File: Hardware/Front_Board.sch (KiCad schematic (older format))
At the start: 15 parts, among them J4 Camera, J5 Motherboard_Right, Q1 DMG3414U

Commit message: [Hardware] Renamed 'camera board' to 'front board' as this board is not only carrying the camera.
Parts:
- J4: value Camera -> Front
- J5: value Motherboard_Right -> Front
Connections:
- net CAMERA_BOARD_LDR renamed FRONT_BOARD_LDR
- net CAMERA_BOARD_LEDS renamed FRONT_BOARD_LEDS
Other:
- note added: "Separate front board."
- note removed: "Camera separate board."
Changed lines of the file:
@@
 P 7350 3850
 F 0 "J5" H 7429 3705 50  0000 L CNN
-F 1 "Motherboard_Right" H 7429 3796 50  0000 L CNN
+F 1 "Front" H 7429 3796 50  0000 L CNN
 F 2 "Connector_PinSocket_2.54mm:PinSocket_1x04_P2.54mm_Vertical" H 7350 3850 50  0001 C CNN
 F 3 "~" H 7350 3850 50  0001 C CNN
@@
 	8200 3300 8450 3300
 Text GLabel 7800 3750 2    50   UnSpc ~ 0
-CAMERA_BOARD_LDR
+FRONT_BOARD_LDR
 Wire Wire Line
 	7800 3750 7550 3750
@@
 Wire Notes Line
 	2500 2550 2500 5250
-Text Notes 5150 5150 0    50   ~ 0
-Camera separate board.
+Text Notes 5350 5150 0    50   ~ 0
+Separate front board.
 Wire Wire Line
 	2850 4700 2850 3900
@@
 	8850 4100 8850 4150
 Text GLabel 9100 4100 2    50   Input ~ 0
-CAMERA_BOARD_LEDS
+FRONT_BOARD_LEDS
 Wire Wire Line
 	8850 4100 9100 4100
@@
 P 5350 3750
 F 0 "J4" H 5430 3787 50  0000 L CNN
-F 1 "Camera" H 5430 3696 50  0000 L CNN
+F 1 "Front" H 5430 3696 50  0000 L CNN
 F 2 "Connector_PinHeader_2.54mm:PinHeader_1x04_P2.54mm_Vertical" H 5350 3750 50  0001 C CNN
 F 3 "~" H 5350 3750 50  0001 C CNN

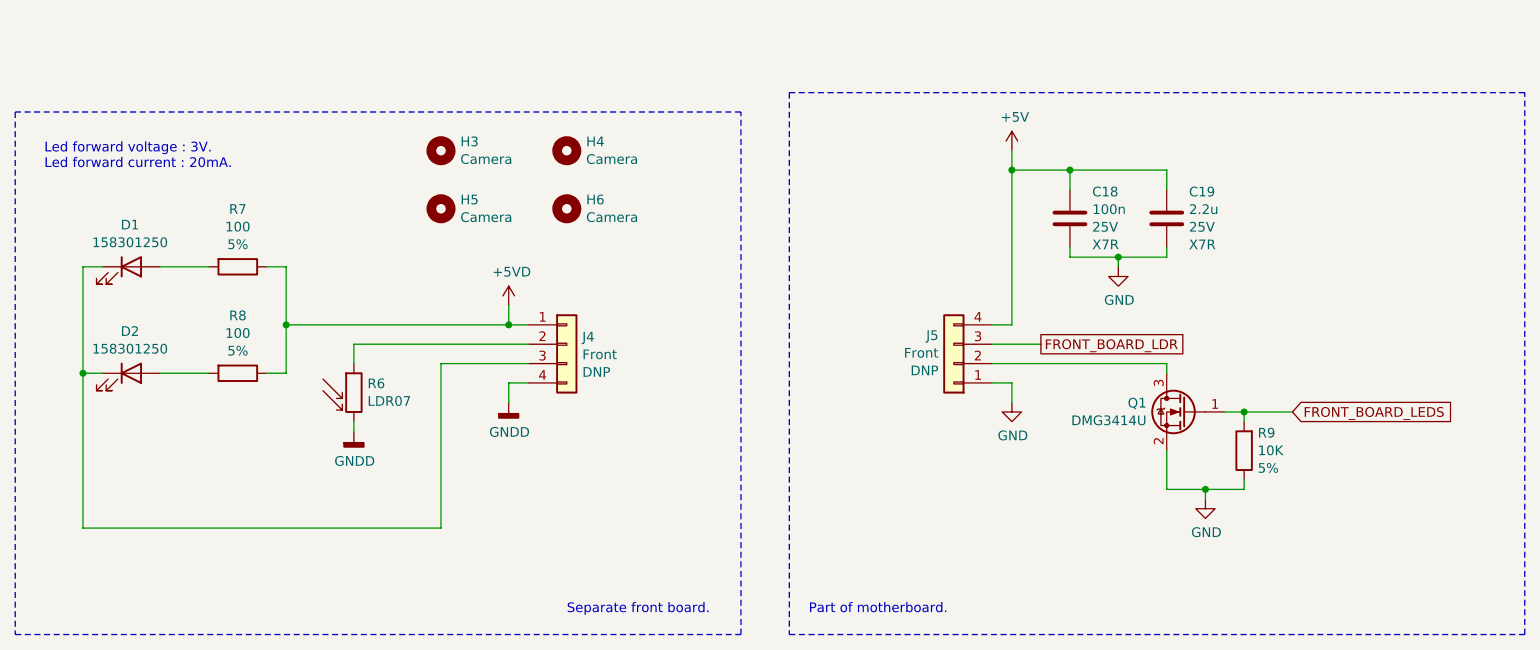
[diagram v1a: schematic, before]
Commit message: [Hardware] Added two more leds for a better night lighting.
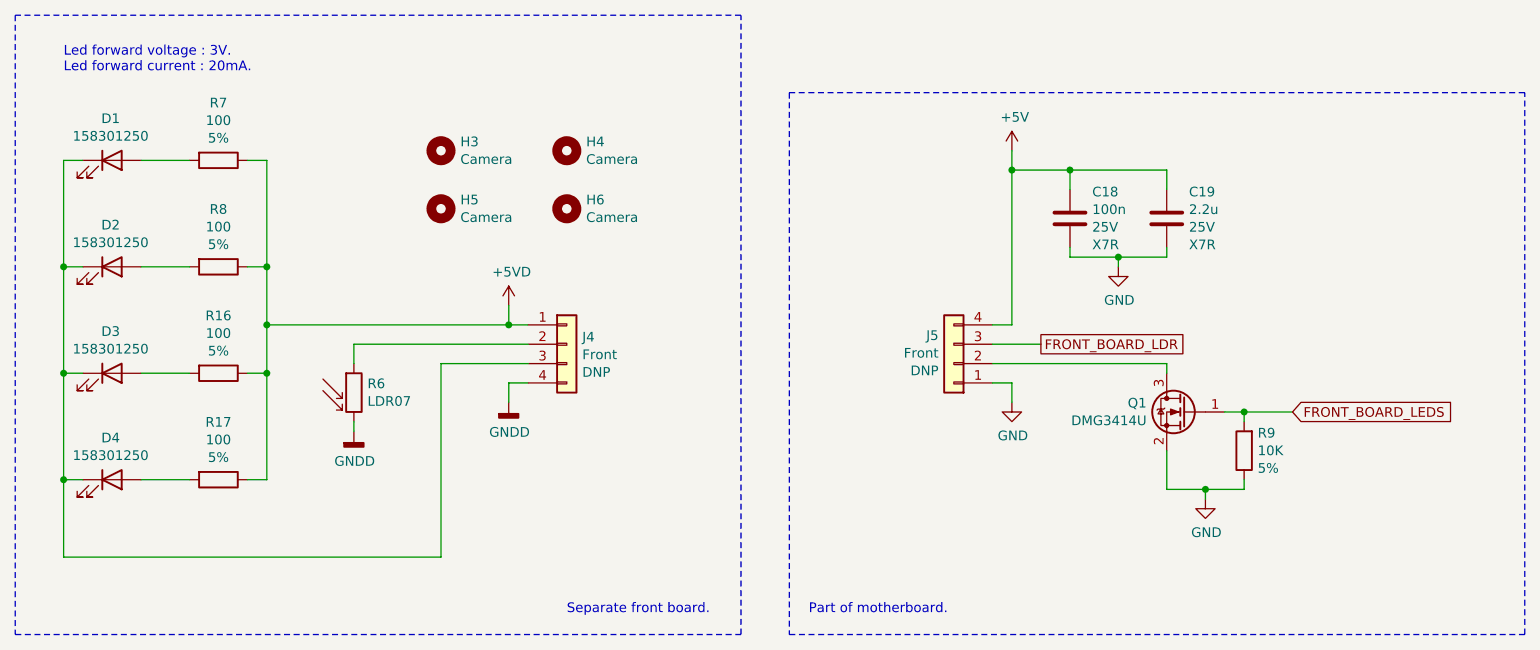
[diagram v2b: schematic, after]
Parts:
- added D3, D4: 158301250, 158301250:158301250, symbol Device:LED
- added R16, R17: 100, Resistor_SMD:R_1206_3216Metric_Pad1.42x1.75mm_HandSolder, symbol Device:R
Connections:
- net +5VD: now also R16.1, R17.1
- net at D1.1 (K), D2.1 (K), J4.3 (Pin_3): now also D3.1 (K), D4.1 (K)
- new net: D3.2 (A), R16.2
- new net: D4.2 (A), R17.2
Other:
- moved on the sheet: D1, D2, R7, R8
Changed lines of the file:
@@
 L Device:LED D1
 U 1 1 5F289A86
-P 3100 3350
-F 0 "D1" H 3093 3566 50  0000 C CNN
-F 1 "158301250" H 3093 3475 50  0000 C CNN
-F 2 "158301250:158301250" H 3100 3350 50  0001 C CNN
-F 3 "~" H 3100 3350 50  0001 C CNN
-	1    3100 3350
+P 3000 2800
+F 0 "D1" H 2993 3016 50  0000 C CNN
+F 1 "158301250" H 2993 2925 50  0000 C CNN
+F 2 "158301250:158301250" H 3000 2800 50  0001 C CNN
+F 3 "~" H 3000 2800 50  0001 C CNN
+	1    3000 2800
 	1    0    0    -1
 $EndComp
@@
 L Device:LED D2
 U 1 1 5F28F949
-P 3100 3900
-F 0 "D2" H 3093 4116 50  0000 C CNN
-F 1 "158301250" H 3093 4025 50  0000 C CNN
-F 2 "158301250:158301250" H 3100 3900 50  0001 C CNN
-F 3 "~" H 3100 3900 50  0001 C CNN
-	1    3100 3900
+P 3000 3350
+F 0 "D2" H 2993 3566 50  0000 C CNN
+F 1 "158301250" H 2993 3475 50  0000 C CNN
+F 2 "158301250:158301250" H 3000 3350 50  0001 C CNN
+F 3 "~" H 3000 3350 50  0001 C CNN
+	1    3000 3350
 	1    0    0    -1
 $EndComp
@@
 Wire Wire Line
 	5050 3650 5150 3650
-Connection ~ 5050 3650
-Wire Wire Line
-	2950 3900 2850 3900
-Wire Wire Line
-	2850 3900 2850 3350
-Wire Wire Line
-	2850 3350 2950 3350
-Text Notes 2650 2850 0    50   ~ 0
+Wire Wire Line
+	2850 3350 2750 3350
+Wire Wire Line
+	2750 3350 2750 2800
+Wire Wire Line
+	2750 2800 2850 2800
+Text Notes 2750 2350 0    50   ~ 0
 Led forward voltage : 3V.\nLed forward current : 20mA.
 $Comp
 L Device:R R7
 U 1 1 5F2D70A9
-P 3650 3350
-F 0 "R7" V 3353 3350 50  0000 C CNN
-F 1 "100" V 3444 3350 50  0000 C CNN
-F 2 "Resistor_SMD:R_1206_3216Metric_Pad1.42x1.75mm_HandSolder" V 3580 3350 50  0001 C CNN
-F 3 "~" H 3650 3350 50  0001 C CNN
-F 4 "5%" V 3535 3350 50  0000 C CNN "Value2"
-	1    3650 3350
+P 3550 2800
+F 0 "R7" V 3253 2800 50  0000 C CNN
+F 1 "100" V 3344 2800 50  0000 C CNN
+F 2 "Resistor_SMD:R_1206_3216Metric_Pad1.42x1.75mm_HandSolder" V 3480 2800 50  0001 C CNN
+F 3 "~" H 3550 2800 50  0001 C CNN
+F 4 "5%" V 3435 2800 50  0000 C CNN "Value2"
+	1    3550 2800
 	0    1    1    0
 $EndComp
@@
 L Device:R R8
 U 1 1 5F2DA263
-P 3650 3900
-F 0 "R8" V 3353 3900 50  0000 C CNN
-F 1 "100" V 3444 3900 50  0000 C CNN
-F 2 "Resistor_SMD:R_1206_3216Metric_Pad1.42x1.75mm_HandSolder" V 3580 3900 50  0001 C CNN
-F 3 "~" H 3650 3900 50  0001 C CNN
-F 4 "5%" V 3535 3900 50  0000 C CNN "Value2"
-	1    3650 3900
+P 3550 3350
+F 0 "R8" V 3253 3350 50  0000 C CNN
+F 1 "100" V 3344 3350 50  0000 C CNN
+F 2 "Resistor_SMD:R_1206_3216Metric_Pad1.42x1.75mm_HandSolder" V 3480 3350 50  0001 C CNN
+F 3 "~" H 3550 3350 50  0001 C CNN
+F 4 "5%" V 3435 3350 50  0000 C CNN "Value2"
+	1    3550 3350
 	0    1    1    0
 $EndComp
 Wire Wire Line
-	3250 3350 3500 3350
-Wire Wire Line
-	3250 3900 3500 3900
-Wire Wire Line
-	3800 3350 3900 3350
-Wire Wire Line
-	3900 3350 3900 3650
-Wire Wire Line
-	3900 3900 3800 3900
-Wire Wire Line
-	3900 3650 5050 3650
-Connection ~ 3900 3650
-Wire Wire Line
-	3900 3650 3900 3900
+	3150 2800 3400 2800
+Wire Wire Line
+	3150 3350 3400 3350
+Wire Wire Line
+	3700 2800 3800 2800
+Wire Wire Line
+	3800 3350 3700 3350
 $Comp
 L Mechanical:MountingHole H3
@@
 	2500 5250 6250 5250
 Wire Notes Line
-	6250 5250 6250 2550
-Wire Notes Line
-	6250 2550 2500 2550
-Wire Notes Line
-	2500 2550 2500 5250
+	6250 5250 6250 2050
+Wire Notes Line
+	6250 2050 2500 2050
+Wire Notes Line
+	2500 2050 2500 5250
 Text Notes 5350 5150 0    50   ~ 0
 Separate front board.
-Wire Wire Line
-	2850 4700 2850 3900
-Connection ~ 2850 3900
+Connection ~ 2750 3350
 $Comp
 L Transistor_FET:DMG3414U Q1
@@
 	4250 3750 4250 3850
 Wire Wire Line
-	4700 3850 4700 4700
-Wire Wire Line
 	4700 3850 5150 3850
-Wire Wire Line
-	4700 4700 2850 4700
 Wire Wire Line
 	7650 2750 7650 2850
@@
 Wire Wire Line
 	7650 3950 7650 4050
+$Comp
+L Device:LED D3
+U 1 1 5F22A727
+P 3000 3900
+F 0 "D3" H 2993 4116 50  0000 C CNN
+F 1 "158301250" H 2993 4025 50  0000 C CNN
+F 2 "158301250:158301250" H 3000 3900 50  0001 C CNN
+F 3 "~" H 3000 3900 50  0001 C CNN
+	1    3000 3900
+	1    0    0    -1
+$EndComp
+$Comp
+L Device:LED D4
+U 1 1 5F22A72D
+P 3000 4450
+F 0 "D4" H 2993 4666 50  0000 C CNN
+F 1 "158301250" H 2993 4575 50  0000 C CNN
+F 2 "158301250:158301250" H 3000 4450 50  0001 C CNN
+F 3 "~" H 3000 4450 50  0001 C CNN
+	1    3000 4450
+	1    0    0    -1
+$EndComp
+Wire Wire Line
+	2850 4450 2750 4450
+$Comp
+L Device:R R16
+U 1 1 5F22A736
+P 3550 3900
+F 0 "R16" V 3253 3900 50  0000 C CNN
+F 1 "100" V 3344 3900 50  0000 C CNN
+F 2 "Resistor_SMD:R_1206_3216Metric_Pad1.42x1.75mm_HandSolder" V 3480 3900 50  0001 C CNN
+F 3 "~" H 3550 3900 50  0001 C CNN
+F 4 "5%" V 3435 3900 50  0000 C CNN "Value2"
+	1    3550 3900
+	0    1    1    0
+$EndComp
+$Comp
+L Device:R R17
+U 1 1 5F22A73D
+P 3550 4450
+F 0 "R17" V 3253 4450 50  0000 C CNN
+F 1 "100" V 3344 4450 50  0000 C CNN
+F 2 "Resistor_SMD:R_1206_3216Metric_Pad1.42x1.75mm_HandSolder" V 3480 4450 50  0001 C CNN
+F 3 "~" H 3550 4450 50  0001 C CNN
+F 4 "5%" V 3435 4450 50  0000 C CNN "Value2"
+	1    3550 4450
+	0    1    1    0
+$EndComp
+Wire Wire Line
+	3150 3900 3400 3900
+Wire Wire Line
+	3150 4450 3400 4450
+Wire Wire Line
+	3700 3900 3800 3900
+Wire Wire Line
+	3800 4450 3700 4450
+Wire Wire Line
+	2850 3900 2750 3900
+Connection ~ 2750 3900
+Wire Wire Line
+	2750 3900 2750 3350
+Wire Wire Line
+	3800 3350 3800 3650
+Connection ~ 3800 3350
+Wire Wire Line
+	3800 3900 3800 4450
+Connection ~ 3800 3900
+Wire Wire Line
+	2750 3900 2750 4450
+Wire Wire Line
+	3800 2800 3800 3350
+Connection ~ 5050 3650
+Wire Wire Line
+	3800 3650 5050 3650
+Connection ~ 3800 3650
+Wire Wire Line
+	3800 3650 3800 3900
+Wire Wire Line
+	2750 4450 2750 4850
+Wire Wire Line
+	2750 4850 4700 4850
+Wire Wire Line
+	4700 3850 4700 4850
+Connection ~ 2750 4450
 $EndSCHEMATC

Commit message: [Hardware] Added front board mounting holes.
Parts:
- added H11, H12: Front_Board, MountingHole:MountingHole_4.3mm_M4, symbol Mechanical:MountingHole
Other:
- moved on the sheet: H3, H4, H5, H6
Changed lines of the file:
@@
 L Mechanical:MountingHole H3
 U 1 1 5F2EC62F
-P 4700 2750
-F 0 "H3" H 4800 2796 50  0000 L CNN
-F 1 "Camera" H 4800 2705 50  0000 L CNN
-F 2 "MountingHole:MountingHole_2.2mm_M2" H 4700 2750 50  0001 C CNN
-F 3 "~" H 4700 2750 50  0001 C CNN
-	1    4700 2750
+P 4500 2350
+F 0 "H3" H 4600 2396 50  0000 L CNN
+F 1 "Camera" H 4600 2305 50  0000 L CNN
+F 2 "MountingHole:MountingHole_2.2mm_M2" H 4500 2350 50  0001 C CNN
+F 3 "~" H 4500 2350 50  0001 C CNN
+	1    4500 2350
 	1    0    0    -1
 $EndComp
@@
 L Mechanical:MountingHole H4
 U 1 1 5F2F030A
-P 5350 2750
-F 0 "H4" H 5450 2796 50  0000 L CNN
-F 1 "Camera" H 5450 2705 50  0000 L CNN
-F 2 "MountingHole:MountingHole_2.2mm_M2" H 5350 2750 50  0001 C CNN
-F 3 "~" H 5350 2750 50  0001 C CNN
-	1    5350 2750
+P 5250 2350
+F 0 "H4" H 5350 2396 50  0000 L CNN
+F 1 "Camera" H 5350 2305 50  0000 L CNN
+F 2 "MountingHole:MountingHole_2.2mm_M2" H 5250 2350 50  0001 C CNN
+F 3 "~" H 5250 2350 50  0001 C CNN
+	1    5250 2350
 	1    0    0    -1
 $EndComp
@@
 L Mechanical:MountingHole H5
 U 1 1 5F2F0621
-P 4700 3050
-F 0 "H5" H 4800 3096 50  0000 L CNN
-F 1 "Camera" H 4800 3005 50  0000 L CNN
-F 2 "MountingHole:MountingHole_2.2mm_M2" H 4700 3050 50  0001 C CNN
-F 3 "~" H 4700 3050 50  0001 C CNN
-	1    4700 3050
+P 4500 2650
+F 0 "H5" H 4600 2696 50  0000 L CNN
+F 1 "Camera" H 4600 2605 50  0000 L CNN
+F 2 "MountingHole:MountingHole_2.2mm_M2" H 4500 2650 50  0001 C CNN
+F 3 "~" H 4500 2650 50  0001 C CNN
+	1    4500 2650
 	1    0    0    -1
 $EndComp
@@
 L Mechanical:MountingHole H6
 U 1 1 5F2F098F
-P 5350 3050
-F 0 "H6" H 5450 3096 50  0000 L CNN
-F 1 "Camera" H 5450 3005 50  0000 L CNN
-F 2 "MountingHole:MountingHole_2.2mm_M2" H 5350 3050 50  0001 C CNN
-F 3 "~" H 5350 3050 50  0001 C CNN
-	1    5350 3050
+P 5250 2650
+F 0 "H6" H 5350 2696 50  0000 L CNN
+F 1 "Camera" H 5350 2605 50  0000 L CNN
+F 2 "MountingHole:MountingHole_2.2mm_M2" H 5250 2650 50  0001 C CNN
+F 3 "~" H 5250 2650 50  0001 C CNN
+	1    5250 2650
 	1    0    0    -1
 $EndComp
@@
 	4700 3850 4700 4850
 Connection ~ 2750 4450
+$Comp
+L Mechanical:MountingHole H11
+U 1 1 5F25DF87
+P 4500 2950
+F 0 "H11" H 4600 2996 50  0000 L CNN
+F 1 "Front_Board" H 4600 2905 50  0000 L CNN
+F 2 "MountingHole:MountingHole_4.3mm_M4" H 4500 2950 50  0001 C CNN
+F 3 "~" H 4500 2950 50  0001 C CNN
+	1    4500 2950
+	1    0    0    -1
+$EndComp
+$Comp
+L Mechanical:MountingHole H12
+U 1 1 5F25EF87
+P 5250 2950
+F 0 "H12" H 5350 2996 50  0000 L CNN
+F 1 "Front_Board" H 5350 2905 50  0000 L CNN
+F 2 "MountingHole:MountingHole_4.3mm_M4" H 5250 2950 50  0001 C CNN
+F 3 "~" H 5250 2950 50  0001 C CNN
+	1    5250 2950
+	1    0    0    -1
+$EndComp
 $EndSCHEMATC

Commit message: [Hardware] Changed front board mounting holes footprint to match angle bracket holes and positionned holes on front board PCB.
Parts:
- H11, H12: footprint MountingHole:MountingHole_4.3mm_M4 -> MountingHole:MountingHole_3.2mm_M3
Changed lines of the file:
@@
 F 0 "H11" H 4600 2996 50  0000 L CNN
 F 1 "Front_Board" H 4600 2905 50  0000 L CNN
-F 2 "MountingHole:MountingHole_4.3mm_M4" H 4500 2950 50  0001 C CNN
+F 2 "MountingHole:MountingHole_3.2mm_M3" H 4500 2950 50  0001 C CNN
 F 3 "~" H 4500 2950 50  0001 C CNN
 	1    4500 2950
@@
 F 0 "H12" H 5350 2996 50  0000 L CNN
 F 1 "Front_Board" H 5350 2905 50  0000 L CNN
-F 2 "MountingHole:MountingHole_4.3mm_M4" H 5250 2950 50  0001 C CNN
+F 2 "MountingHole:MountingHole_3.2mm_M3" H 5250 2950 50  0001 C CNN
 F 3 "~" H 5250 2950 50  0001 C CNN
 	1    5250 2950

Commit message: [Hardware] Added test breaking tabs to PCB to be able to determine PCB production needs.
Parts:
- added BT1, BT2: BreakTab, Break_Tab:Break_Tab, symbol Mechanical:MountingHole
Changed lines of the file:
@@
+	1    0    0    -1
+$EndComp
+$Comp
+L Mechanical:MountingHole BT1
+U 1 1 5F3734C7
+P 5350 4500
+F 0 "BT1" H 5450 4546 50  0000 L CNN
+F 1 "BreakTab" H 5450 4455 50  0000 L CNN
+F 2 "Break_Tab:Break_Tab" H 5350 4500 50  0001 C CNN
+F 3 "~" H 5350 4500 50  0001 C CNN
+	1    5350 4500
+	1    0    0    -1
+$EndComp
+$Comp
+L Mechanical:MountingHole BT2
+U 1 1 5F375442
+P 5350 4750
+F 0 "BT2" H 5450 4796 50  0000 L CNN
+F 1 "BreakTab" H 5450 4705 50  0000 L CNN
+F 2 "Break_Tab:Break_Tab" H 5350 4750 50  0001 C CNN
+F 3 "~" H 5350 4750 50  0001 C CNN
+	1    5350 4750
 	1    0    0    -1
 $EndComp

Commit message: [Hardware] Fixed bad footprints and duplicated break tab footprints.
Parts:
- added BT3, BT4, BT5, BT6: BreakTab, Break_Tab:Break_Tab, symbol Mechanical:MountingHole
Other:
- moved on the sheet: BT1
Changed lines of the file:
@@
 L Mechanical:MountingHole BT1
 U 1 1 5F3734C7
-P 5350 4500
-F 0 "BT1" H 5450 4546 50  0000 L CNN
-F 1 "BreakTab" H 5450 4455 50  0000 L CNN
-F 2 "Break_Tab:Break_Tab" H 5350 4500 50  0001 C CNN
-F 3 "~" H 5350 4500 50  0001 C CNN
-	1    5350 4500
+P 5550 4300
+F 0 "BT1" H 5650 4346 50  0000 L CNN
+F 1 "BreakTab" H 5650 4255 50  0000 L CNN
+F 2 "Break_Tab:Break_Tab" H 5550 4300 50  0001 C CNN
+F 3 "~" H 5550 4300 50  0001 C CNN
+	1    5550 4300
 	1    0    0    -1
 $EndComp
 $Comp
 L Mechanical:MountingHole BT2
-U 1 1 5F375442
-P 5350 4750
-F 0 "BT2" H 5450 4796 50  0000 L CNN
-F 1 "BreakTab" H 5450 4705 50  0000 L CNN
-F 2 "Break_Tab:Break_Tab" H 5350 4750 50  0001 C CNN
-F 3 "~" H 5350 4750 50  0001 C CNN
-	1    5350 4750
+U 1 1 5F3A13DD
+P 5550 4550
+F 0 "BT2" H 5650 4596 50  0000 L CNN
+F 1 "BreakTab" H 5650 4505 50  0000 L CNN
+F 2 "Break_Tab:Break_Tab" H 5550 4550 50  0001 C CNN
+F 3 "~" H 5550 4550 50  0001 C CNN
+	1    5550 4550
 	1    0    0    -1
 $EndComp
+$Comp
+L Mechanical:MountingHole BT3
+U 1 1 5F3A17F1
+P 5550 4800
+F 0 "BT3" H 5650 4846 50  0000 L CNN
+F 1 "BreakTab" H 5650 4755 50  0000 L CNN
+F 2 "Break_Tab:Break_Tab" H 5550 4800 50  0001 C CNN
+F 3 "~" H 5550 4800 50  0001 C CNN
+	1    5550 4800
+	1    0    0    -1
+$EndComp
+$Comp
+L Mechanical:MountingHole BT4
+U 1 1 5F3ABA27
+P 6800 4300
+F 0 "BT4" H 6900 4346 50  0000 L CNN
+F 1 "BreakTab" H 6900 4255 50  0000 L CNN
+F 2 "Break_Tab:Break_Tab" H 6800 4300 50  0001 C CNN
+F 3 "~" H 6800 4300 50  0001 C CNN
+	1    6800 4300
+	1    0    0    -1
+$EndComp
+$Comp
+L Mechanical:MountingHole BT5
+U 1 1 5F3ABA2D
+P 6800 4550
+F 0 "BT5" H 6900 4596 50  0000 L CNN
+F 1 "BreakTab" H 6900 4505 50  0000 L CNN
+F 2 "Break_Tab:Break_Tab" H 6800 4550 50  0001 C CNN
+F 3 "~" H 6800 4550 50  0001 C CNN
+	1    6800 4550
+	1    0    0    -1
+$EndComp
+$Comp
+L Mechanical:MountingHole BT6
+U 1 1 5F3ABA33
+P 6800 4800
+F 0 "BT6" H 6900 4846 50  0000 L CNN
+F 1 "BreakTab" H 6900 4755 50  0000 L CNN
+F 2 "Break_Tab:Break_Tab" H 6800 4800 50  0001 C CNN
+F 3 "~" H 6800 4800 50  0001 C CNN
+	1    6800 4800
+	1    0    0    -1
+$EndComp

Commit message: [Hardware] Changed motherboard connector to front board footprint and added more marking to motherboard PCB.
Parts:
- J5: footprint Connector_PinSocket_2.54mm:PinSocket_1x04_P2.54mm_Vertical -> Connector_PinHeader_2.54mm:PinHeader_1x04_P2.54mm_Vertical
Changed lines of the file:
@@
 F 0 "J5" H 7429 3705 50  0000 L CNN
 F 1 "Front" H 7429 3796 50  0000 L CNN
-F 2 "Connector_PinSocket_2.54mm:PinSocket_1x04_P2.54mm_Vertical" H 7350 3850 50  0001 C CNN
+F 2 "Connector_PinHeader_2.54mm:PinHeader_1x04_P2.54mm_Vertical" H 7350 3850 50  0001 C CNN
 F 3 "~" H 7350 3850 50  0001 C CNN
 F 4 "DNP" H 7429 3887 50  0000 L CNN "Populate"
